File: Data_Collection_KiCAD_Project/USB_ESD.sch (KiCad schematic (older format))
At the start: 12 parts

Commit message: Fixed Component Libraries
Changed over from project specific to global libraries.
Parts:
- C? (x2): symbol Data_Collection_KiCAD_Project-rescue:C-Device -> Data_Collection_KiCAD_Project-rescue:C-Device-Data_Collection_KiCAD_Project-rescue
- D?: symbol Data_Collection_KiCAD_Project-rescue:LED-Device -> Data_Collection_KiCAD_Project-rescue:LED-Device-Data_Collection_KiCAD_Project-rescue
- D? (x2): symbol Data_Collection_KiCAD_Project-rescue:D_Zener-Device -> Data_Collection_KiCAD_Project-rescue:D_Zener-Device-Data_Collection_KiCAD_Project-rescue
- FB?: symbol Data_Collection_KiCAD_Project-rescue:Ferrite_Bead_Small-Device -> Data_Collection_KiCAD_Project-rescue:Ferrite_Bead_Small-Device-Data_Collection_KiCAD_Project-rescue
- J?: symbol Data_Collection_KiCAD_Project-rescue:USB_B_Micro-Connector -> Data_Collection_KiCAD_Project-rescue:USB_B_Micro-Connector-Data_Collection_KiCAD_Project-rescue
- R? (x3): symbol Data_Collection_KiCAD_Project-rescue:R-Device -> Data_Collection_KiCAD_Project-rescue:R-Device-Data_Collection_KiCAD_Project-rescue
- U?: symbol Data_Collection_KiCAD_Project-rescue:USBLC6-2SC6-Power_Protection -> Data_Collection_KiCAD_Project-rescue:USBLC6-2SC6-Power_Protection-Data_Collection_KiCAD_Project-rescue
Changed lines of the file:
@@
 $Descr A4 11693 8268
 encoding utf-8
-Sheet 2 10
+Sheet 2 9
 Title "USB Connector and ESD Protection"
 Date "2021-10-01"
@@
 $EndDescr
 $Comp
-L Data_Collection_KiCAD_Project-rescue:USB_B_Micro-Connector J?
+L Data_Collection_KiCAD_Project-rescue:USB_B_Micro-Connector-Data_Collection_KiCAD_Project-rescue J?
 U 1 1 616146B0
 P 2150 3950
@@
 $EndComp
 $Comp
-L Data_Collection_KiCAD_Project-rescue:GND-power #PWR?
+L Data_Collection_KiCAD_Project-rescue:GND-power-Data_Collection_KiCAD_Project-rescue #PWR?
 U 1 1 616146B6
 P 2150 4350
@@
 NoConn ~ 2450 4150
 $Comp
-L Data_Collection_KiCAD_Project-rescue:+5V-power #PWR?
+L Data_Collection_KiCAD_Project-rescue:+5V-power-Data_Collection_KiCAD_Project-rescue #PWR?
 U 1 1 616146BE
 P 3300 3350
@@
 $EndComp
 $Comp
-L Data_Collection_KiCAD_Project-rescue:USBLC6-2SC6-Power_Protection U?
+L Data_Collection_KiCAD_Project-rescue:USBLC6-2SC6-Power_Protection-Data_Collection_KiCAD_Project-rescue U?
 U 1 1 616146C5
 P 7400 4050
@@
 $EndComp
 $Comp
-L Data_Collection_KiCAD_Project-rescue:GND-power #PWR?
+L Data_Collection_KiCAD_Project-rescue:GND-power-Data_Collection_KiCAD_Project-rescue #PWR?
 U 1 1 616146CD
 P 7400 4450
@@
 $EndComp
 $Comp
-L Data_Collection_KiCAD_Project-rescue:+5V-power #PWR?
+L Data_Collection_KiCAD_Project-rescue:+5V-power-Data_Collection_KiCAD_Project-rescue #PWR?
 U 1 1 616146D7
 P 7400 3650
@@
 D-
 $Comp
-L Data_Collection_KiCAD_Project-rescue:Ferrite_Bead_Small-Device FB?
+L Data_Collection_KiCAD_Project-rescue:Ferrite_Bead_Small-Device-Data_Collection_KiCAD_Project-rescue FB?
 U 1 1 617A596A
 P 2800 3750
@@
 	5100 3900 5100 3750
 $Comp
-L Data_Collection_KiCAD_Project-rescue:C-Device C?
+L Data_Collection_KiCAD_Project-rescue:C-Device-Data_Collection_KiCAD_Project-rescue C?
 U 1 1 617B9DBE
 P 5100 4050
@@
 	3900 3900 3900 3750
 $Comp
-L Data_Collection_KiCAD_Project-rescue:C-Device C?
+L Data_Collection_KiCAD_Project-rescue:C-Device-Data_Collection_KiCAD_Project-rescue C?
 U 1 1 617B9DD7
 P 3900 4050
@@
 Connection ~ 5100 3750
 $Comp
-L Data_Collection_KiCAD_Project-rescue:R-Device R?
+L Data_Collection_KiCAD_Project-rescue:R-Device-Data_Collection_KiCAD_Project-rescue R?
 U 1 1 617B9DEE
 P 4750 3950
@@
 $EndComp
 $Comp
-L Data_Collection_KiCAD_Project-rescue:R-Device R?
+L Data_Collection_KiCAD_Project-rescue:R-Device-Data_Collection_KiCAD_Project-rescue R?
 U 1 1 617B9DF4
 P 4400 4350
@@
 LM317 Equation:\nVout = 1.25(1 + R2/R1)\nLet R1 = 240Ω, Vout = 3.3V\nR1 = 393.6Ω ≈ 390Ω
 $Comp
-L Data_Collection_KiCAD_Project-rescue:+3.3V-power #PWR?
+L Data_Collection_KiCAD_Project-rescue:+3.3V-power-Data_Collection_KiCAD_Project-rescue #PWR?
 U 1 1 617BD52E
 P 5100 2900
@@
 $EndComp
 $Comp
-L Data_Collection_KiCAD_Project-rescue:LED-Device D?
+L Data_Collection_KiCAD_Project-rescue:LED-Device-Data_Collection_KiCAD_Project-rescue D?
 U 1 1 617BEEA5
 P 5650 3750
@@
 $EndComp
 $Comp
-L Data_Collection_KiCAD_Project-rescue:R-Device R?
+L Data_Collection_KiCAD_Project-rescue:R-Device-Data_Collection_KiCAD_Project-rescue R?
 U 1 1 617BF66F
 P 6000 4150
@@
 	6000 3750 5800 3750
 $Comp
-L Data_Collection_KiCAD_Project-rescue:GND-power #PWR?
+L Data_Collection_KiCAD_Project-rescue:GND-power-Data_Collection_KiCAD_Project-rescue #PWR?
 U 1 1 617B9DC9
 P 4400 4500
@@
 $EndComp
 $Comp
-L Data_Collection_KiCAD_Project-rescue:GND-power #PWR?
+L Data_Collection_KiCAD_Project-rescue:GND-power-Data_Collection_KiCAD_Project-rescue #PWR?
 U 1 1 617C00BC
 P 3900 4200
@@
 $EndComp
 $Comp
-L Data_Collection_KiCAD_Project-rescue:GND-power #PWR?
+L Data_Collection_KiCAD_Project-rescue:GND-power-Data_Collection_KiCAD_Project-rescue #PWR?
 U 1 1 617C0723
 P 5100 4200
@@
 $EndComp
 $Comp
-L Data_Collection_KiCAD_Project-rescue:GND-power #PWR?
+L Data_Collection_KiCAD_Project-rescue:GND-power-Data_Collection_KiCAD_Project-rescue #PWR?
 U 1 1 617C0CB1
 P 6000 4300
@@
 USB shield to remain floating for USB Devices\nCan be connected to board enclosure if possible
 $Comp
-L Data_Collection_KiCAD_Project-rescue:D_Zener-Device D?
+L Data_Collection_KiCAD_Project-rescue:D_Zener-Device-Data_Collection_KiCAD_Project-rescue D?
 U 1 1 617F9817
 P 3500 3750
@@
 	3300 3750 2900 3750
 $Comp
-L Data_Collection_KiCAD_Project-rescue:D_Zener-Device D?
+L Data_Collection_KiCAD_Project-rescue:D_Zener-Device-Data_Collection_KiCAD_Project-rescue D?
 U 1 1 617FB0E6
 P 4400 3300

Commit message: i2c Pullups added
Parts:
- removed D? (x2): D_Zener, symbol Data_Collection_KiCAD_Project-rescue:D_Zener-Device-Data_Collection_KiCAD_Proje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
- added D? (x2): D, symbol Device:D
- R?: value 1k5 -> 1k5 ?????
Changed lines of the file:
@@
 AR Path="/615EE01A/617BF66F" Ref="R?"  Part="1"
 F 0 "R?" H 6070 4196 50  0000 L CNN
-F 1 "1k5" H 6070 4105 50  0000 L CNN
+F 1 "1k5 ?????" H 6070 4105 50  0000 L CNN
 F 2 "" V 5930 4150 50  0001 C CNN
 F 3 "~" H 6000 4150 50  0001 C CNN
@@
 Text Notes 1600 4850 0    50   ~ 0
 USB shield to remain floating for USB Devices\nCan be connected to board enclosure if possible
-$Comp
-L Data_Collection_KiCAD_Project-rescue:D_Zener-Device-Data_Collection_KiCAD_Project-rescue D?
-U 1 1 617F9817
-P 3500 3750
-F 0 "D?" H 3500 3533 50  0000 C CNN
-F 1 "D_Zener" H 3500 3624 50  0000 C CNN
-F 2 "" H 3500 3750 50  0001 C CNN
-F 3 "~" H 3500 3750 50  0001 C CNN
-	1    3500 3750
-	-1   0    0    1
-$EndComp
 Wire Wire Line
 	3650 3750 3900 3750
@@
 Wire Wire Line
 	3300 3750 2900 3750
-$Comp
-L Data_Collection_KiCAD_Project-rescue:D_Zener-Device-Data_Collection_KiCAD_Project-rescue D?
-U 1 1 617FB0E6
-P 4400 3300
-F 0 "D?" H 4400 3517 50  0000 C CNN
-F 1 "D_Zener" H 4400 3426 50  0000 C CNN
-F 2 "" H 4400 3300 50  0001 C CNN
-F 3 "~" H 4400 3300 50  0001 C CNN
-	1    4400 3300
-	1    0    0    -1
-$EndComp
 Wire Wire Line
 	4550 3300 4750 3300
@@
 Wire Wire Line
 	5100 2900 5100 3750
+$Comp
+L Device:D D?
+U 1 1 619DA3D1
+P 4400 3300
+F 0 "D?" H 4400 3517 50  0000 C CNN
+F 1 "D" H 4400 3426 50  0000 C CNN
+F 2 "" H 4400 3300 50  0001 C CNN
+F 3 "~" H 4400 3300 50  0001 C CNN
+	1    4400 3300
+	1    0    0    -1
+$EndComp
+$Comp
+L Device:D D?
+U 1 1 619DB167
+P 3500 3750
+F 0 "D?" H 3500 3533 50  0000 C CNN
+F 1 "D" H 3500 3624 50  0000 C CNN
+F 2 "" H 3500 3750 50  0001 C CNN
+F 3 "~" H 3500 3750 50  0001 C CNN
+	1    3500 3750
+	-1   0    0    1
+$EndComp
 $EndSCHEMATC

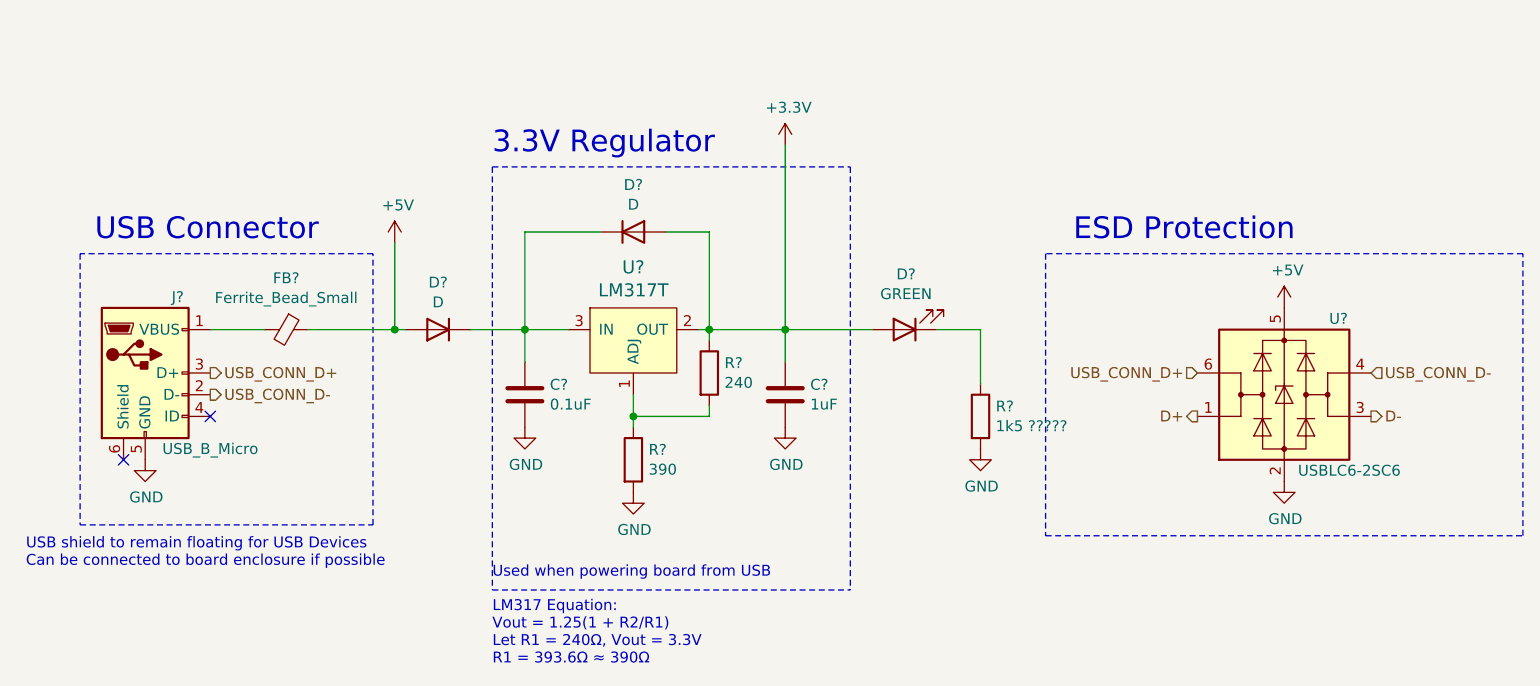
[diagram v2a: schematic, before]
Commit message: footprint and value changes
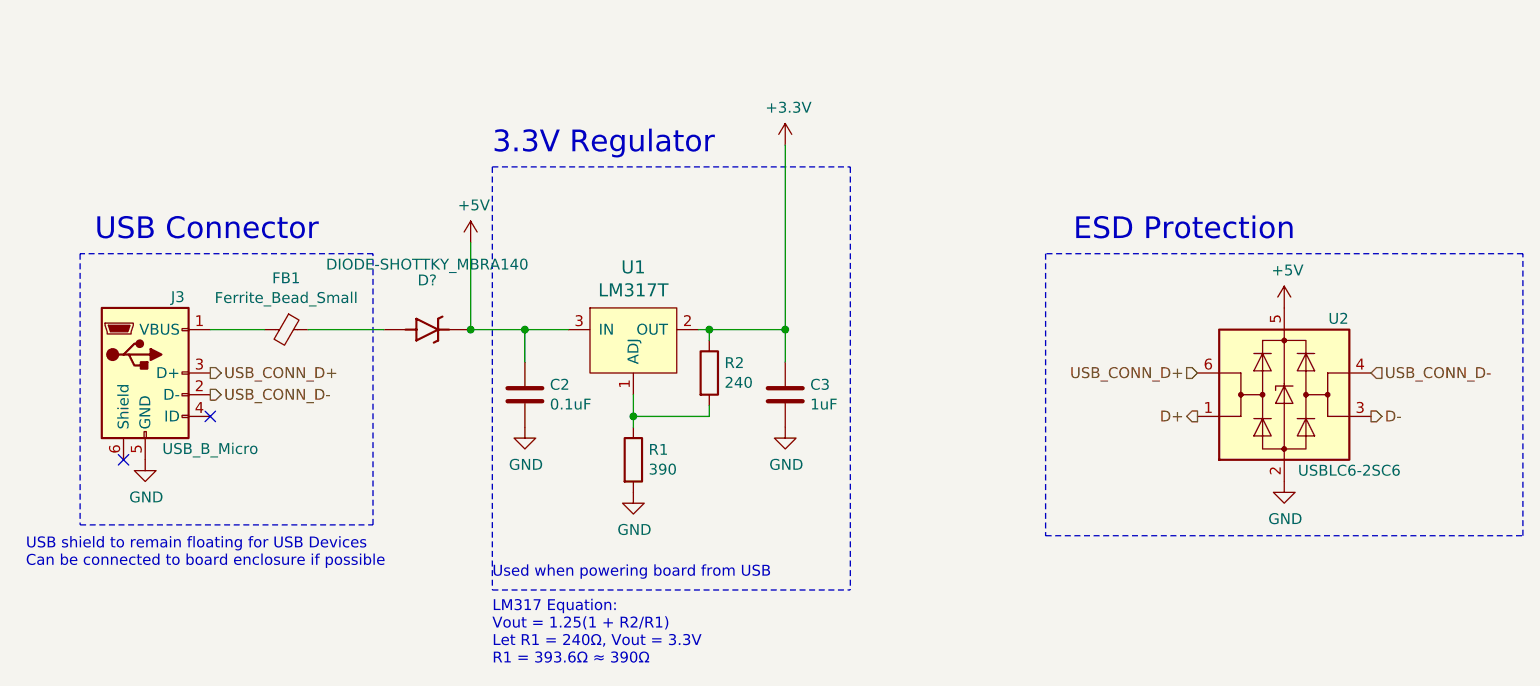
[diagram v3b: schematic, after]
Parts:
- removed D?: GREEN, symbol Data_Collection_KiCAD_Project-rescue:LED-Device-Data_Collection_KiCAD_Project-r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
- removed D? (x2): D, symbol Device:D
- removed R?: 1k5 ?????, symbol Data_Collection_KiCAD_Project-rescue:R-Device-Data_Collection_KiCAD_Project-res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
- added D?: DIODE-SHOTTKY_MBRA140, Silicon-Standard:SMA-DIODE, symbol SparkFun-DiscreteSemi:DIODE-SHOTTKY_MBRA140
- C2, C3: renamed from C?; footprint (none) -> Capacitor_SMD:C_0603_1608Metric
- R1, R2: renamed from R?; footprint (none) -> Resistor_SMD:R_0603_1608Metric
- gave numbers to parts that had none: 4
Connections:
- net +5V: now also C2.1, U1.3 (IN), D?.C; no longer FB1.1
- new net: D?.A, FB1.1

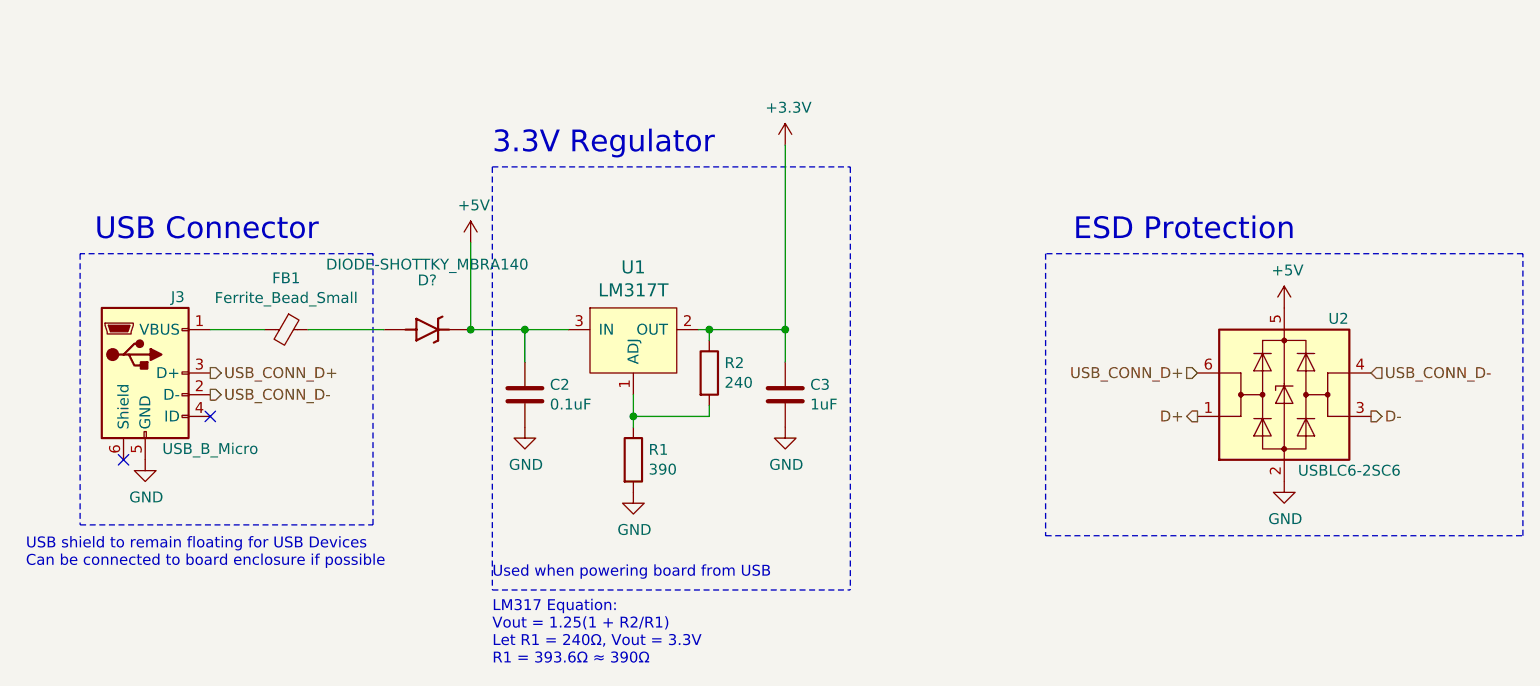
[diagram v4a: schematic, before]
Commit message: footprint changes
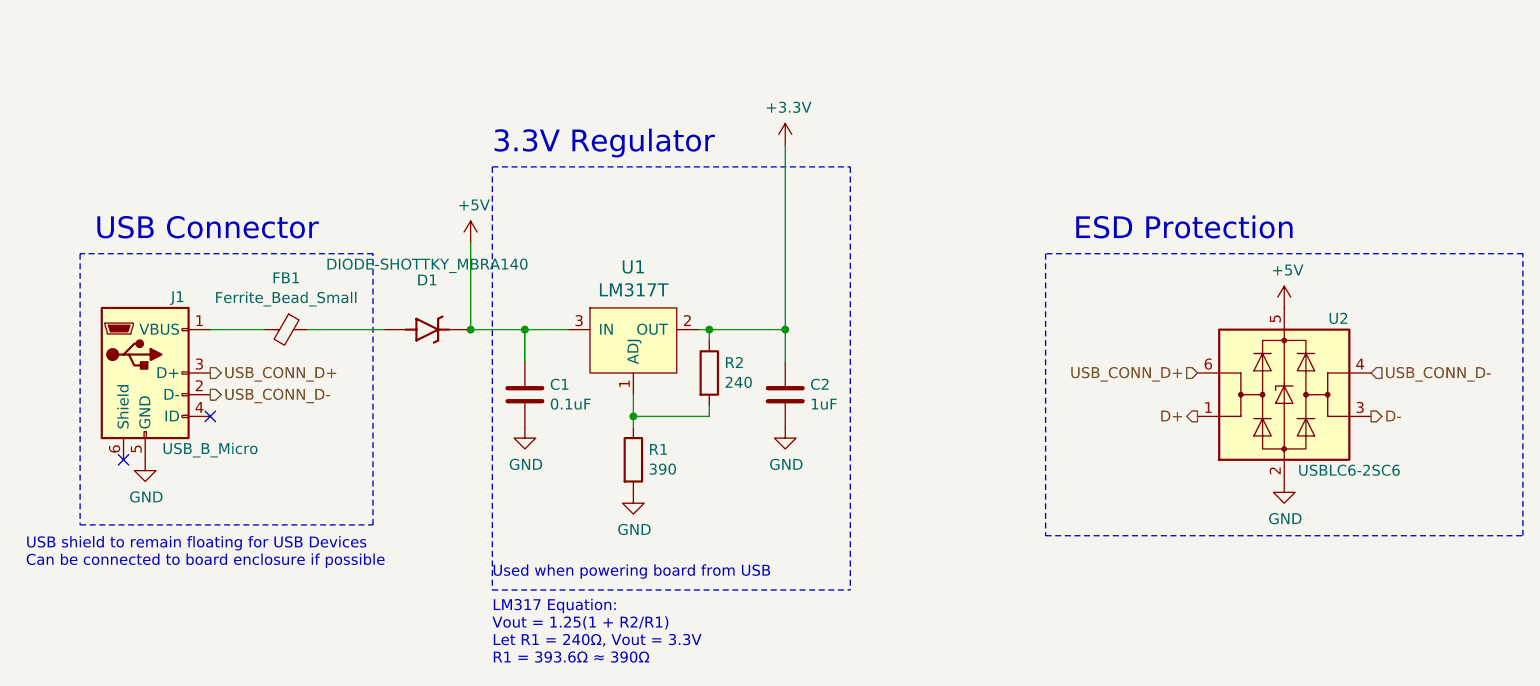
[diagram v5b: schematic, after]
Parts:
- gave numbers to parts that had none: 1
- renumbered C2 to C1, C3 to C2, J3 to J1
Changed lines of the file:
@@
 $EndDescr
 $Comp
-L Data_Collection_KiCAD_Project-rescue:USB_B_Micro-Connector-Data_Collection_KiCAD_Project-rescue J3
+L Data_Collection_KiCAD_Project-rescue:USB_B_Micro-Connector-Data_Collection_KiCAD_Project-rescue J1
 U 1 1 616146B0
 P 2150 3950
-F 0 "J3" H 2300 4300 50  0000 C CNN
+F 0 "J1" H 2300 4300 50  0000 C CNN
 F 1 "USB_B_Micro" H 2450 3600 50  0000 C CNN
 F 2 "" H 2300 3900 50  0001 C CNN
@@
 $EndComp
 $Comp
-L Data_Collection_KiCAD_Project-rescue:GND-power-Data_Collection_KiCAD_Project-rescue #PWR012
+L Data_Collection_KiCAD_Project-rescue:GND-power-Data_Collection_KiCAD_Project-rescue #PWR05
 U 1 1 616146B6
 P 2150 4350
-F 0 "#PWR012" H 2150 4100 50  0001 C CNN
+F 0 "#PWR05" H 2150 4100 50  0001 C CNN
 F 1 "GND" H 2155 4177 50  0000 C CNN
 F 2 "" H 2150 4350 50  0001 C CNN
@@
 NoConn ~ 2450 4150
 $Comp
-L Data_Collection_KiCAD_Project-rescue:+5V-power-Data_Collection_KiCAD_Project-rescue #PWR013
+L Data_Collection_KiCAD_Project-rescue:+5V-power-Data_Collection_KiCAD_Project-rescue #PWR06
 U 1 1 616146BE
 P 3650 3350
-F 0 "#PWR013" H 3650 3200 50  0001 C CNN
+F 0 "#PWR06" H 3650 3200 50  0001 C CNN
 F 1 "+5V" H 3665 3523 50  0000 C CNN
 F 2 "" H 3650 3350 50  0001 C CNN
@@
 $EndComp
 $Comp
-L Data_Collection_KiCAD_Project-rescue:GND-power-Data_Collection_KiCAD_Project-rescue #PWR019
+L Data_Collection_KiCAD_Project-rescue:GND-power-Data_Collection_KiCAD_Project-rescue #PWR012
 U 1 1 616146CD
 P 7400 4450
-F 0 "#PWR019" H 7400 4200 50  0001 C CNN
+F 0 "#PWR012" H 7400 4200 50  0001 C CNN
 F 1 "GND" H 7405 4277 50  0000 C CNN
 F 2 "" H 7400 4450 50  0001 C CNN
@@
 $EndComp
 $Comp
-L Data_Collection_KiCAD_Project-rescue:+5V-power-Data_Collection_KiCAD_Project-rescue #PWR018
+L Data_Collection_KiCAD_Project-rescue:+5V-power-Data_Collection_KiCAD_Project-rescue #PWR011
 U 1 1 616146D7
 P 7400 3650
-F 0 "#PWR018" H 7400 3500 50  0001 C CNN
+F 0 "#PWR011" H 7400 3500 50  0001 C CNN
 F 1 "+5V" H 7415 3823 50  0000 C CNN
 F 2 "" H 7400 3650 50  0001 C CNN
@@
 AR Path="/617B9DBE" Ref="C?"  Part="1"
 AR Path="/615A5159/617B9DBE" Ref="C?"  Part="1"
-AR Path="/615EE01A/617B9DBE" Ref="C3"  Part="1"
-F 0 "C3" H 5215 4096 50  0000 L CNN
+AR Path="/615EE01A/617B9DBE" Ref="C2"  Part="1"
+F 0 "C2" H 5215 4096 50  0000 L CNN
 F 1 "1uF" H 5215 4005 50  0000 L CNN
 F 2 "Capacitor_SMD:C_0603_1608Metric" H 5138 3900 50  0001 C CNN
@@
 AR Path="/617B9DD7" Ref="C?"  Part="1"
 AR Path="/615A5159/617B9DD7" Ref="C?"  Part="1"
-AR Path="/615EE01A/617B9DD7" Ref="C2"  Part="1"
-F 0 "C2" H 4015 4096 50  0000 L CNN
+AR Path="/615EE01A/617B9DD7" Ref="C1"  Part="1"
+F 0 "C1" H 4015 4096 50  0000 L CNN
 F 1 "0.1uF" H 4015 4005 50  0000 L CNN
 F 2 "Capacitor_SMD:C_0603_1608Metric" H 3938 3900 50  0001 C CNN
@@
 P 5100 2900
 AR Path="/617BD52E" Ref="#PWR?"  Part="1"
-AR Path="/615EE01A/617BD52E" Ref="#PWR016"  Part="1"
-F 0 "#PWR016" H 5100 2750 50  0001 C CNN
+AR Path="/615EE01A/617BD52E" Ref="#PWR09"  Part="1"
+F 0 "#PWR09" H 5100 2750 50  0001 C CNN
 F 1 "+3.3V" H 5115 3073 50  0000 C CNN
 F 2 "" H 5100 2900 50  0001 C CNN
@@
 AR Path="/617B9DC9" Ref="#PWR?"  Part="1"
 AR Path="/615A5159/617B9DC9" Ref="#PWR?"  Part="1"
-AR Path="/615EE01A/617B9DC9" Ref="#PWR015"  Part="1"
-F 0 "#PWR015" H 4400 4250 50  0001 C CNN
+AR Path="/615EE01A/617B9DC9" Ref="#PWR08"  Part="1"
+F 0 "#PWR08" H 4400 4250 50  0001 C CNN
 F 1 "GND" H 4405 4327 50  0000 C CNN
 F 2 "" H 4400 4500 50  0001 C CNN
@@
 AR Path="/617C00BC" Ref="#PWR?"  Part="1"
 AR Path="/615A5159/617C00BC" Ref="#PWR?"  Part="1"
-AR Path="/615EE01A/617C00BC" Ref="#PWR014"  Part="1"
-F 0 "#PWR014" H 3900 3950 50  0001 C CNN
+AR Path="/615EE01A/617C00BC" Ref="#PWR07"  Part="1"
+F 0 "#PWR07" H 3900 3950 50  0001 C CNN
 F 1 "GND" H 3905 4027 50  0000 C CNN
 F 2 "" H 3900 4200 50  0001 C CNN
@@
 AR Path="/617C0723" Ref="#PWR?"  Part="1"
 AR Path="/615A5159/617C0723" Ref="#PWR?"  Part="1"
-AR Path="/615EE01A/617C0723" Ref="#PWR017"  Part="1"
-F 0 "#PWR017" H 5100 3950 50  0001 C CNN
+AR Path="/615EE01A/617C0723" Ref="#PWR010"  Part="1"
+F 0 "#PWR010" H 5100 3950 50  0001 C CNN
 F 1 "GND" H 5105 4027 50  0000 C CNN
 F 2 "" H 5100 4200 50  0001 C CNN
@@
 	5100 2900 5100 3750
 $Comp
-L SparkFun-DiscreteSemi:DIODE-SHOTTKY_MBRA140 D?
+L SparkFun-DiscreteSemi:DIODE-SHOTTKY_MBRA140 D1
 U 1 1 61A08B7E
 P 3450 3750
-F 0 "D?" H 3450 3977 50  0000 C CNN
+F 0 "D1" H 3450 3977 50  0000 C CNN
 F 1 "DIODE-SHOTTKY_MBRA140" H 3450 4050 50  0000 C CNN
 F 2 "Silicon-Standard:SMA-DIODE" H 4100 3600 50  0001 C CNN
